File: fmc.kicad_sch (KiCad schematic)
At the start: 2 parts, among them P1 ASP-134604-01, P2 ASP-134604-01

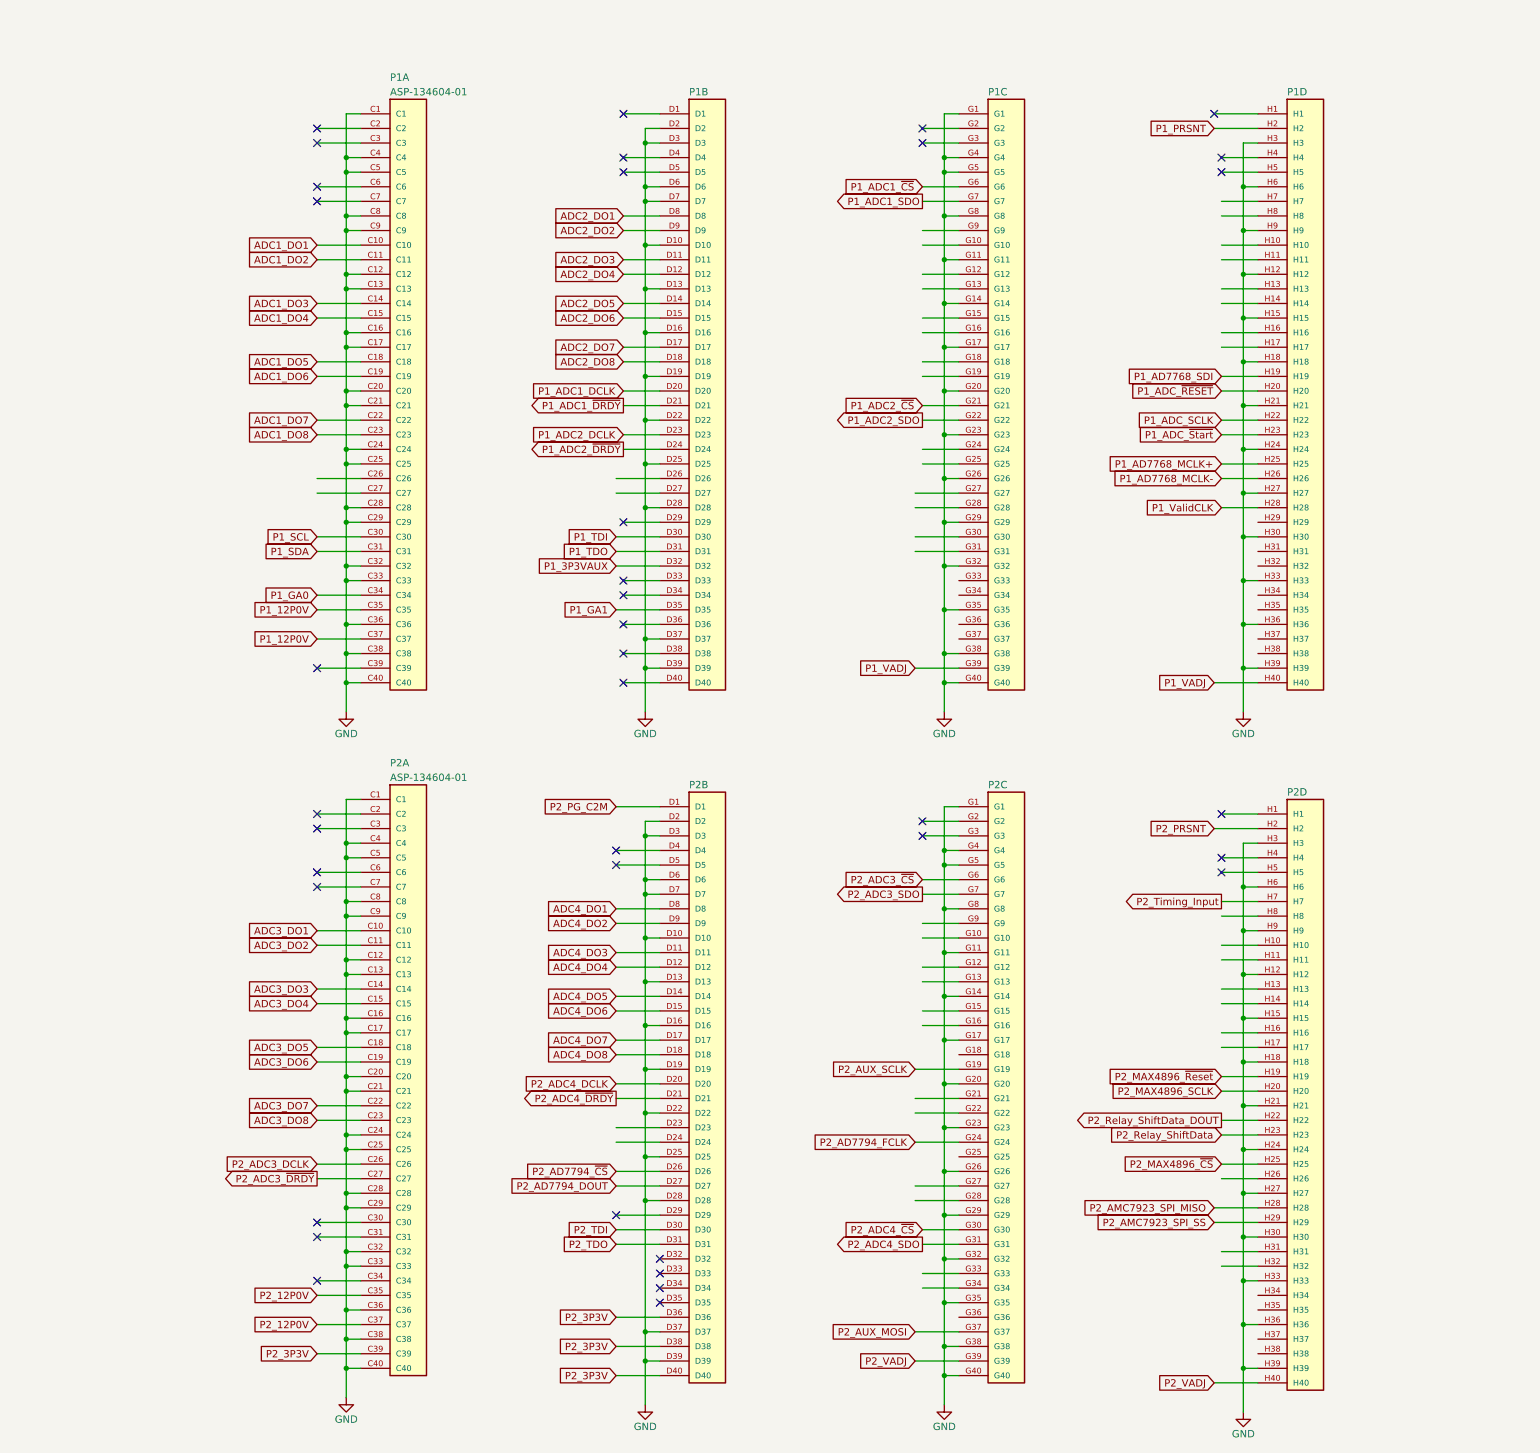
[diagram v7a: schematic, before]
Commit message: Schematic Updates
Updated:
-Fixed AMC7823 labels
-Added present detect signals on FMC
-Added ferrite beads in Power Section and AFE
-Added 0R in power section
-Revised EEPROM connections
-Changed +5V SMPS part to one with an integrated inductor
-Added more detail on FMC connector
-Added file showing SMPS calculations
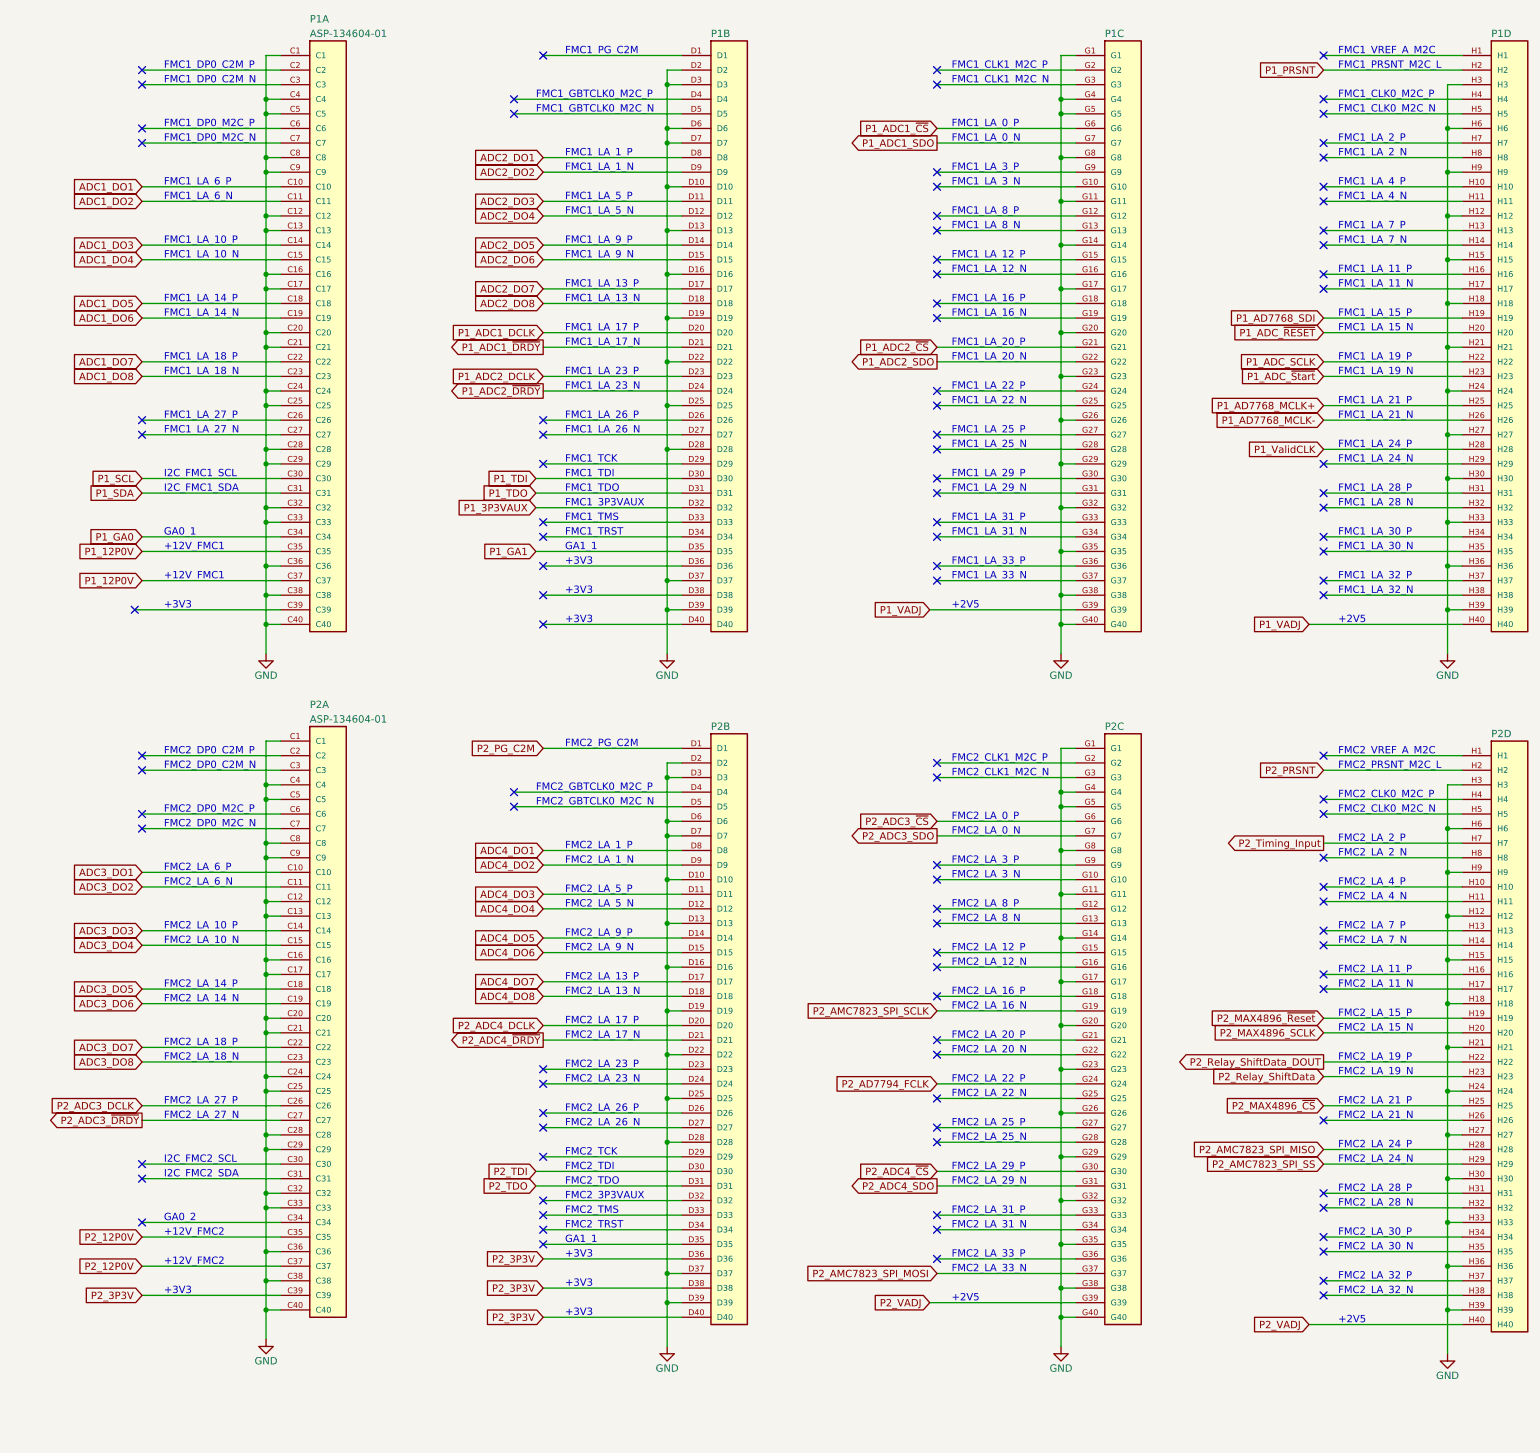
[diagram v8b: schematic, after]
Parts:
- P1, P2: MPN (none) -> ASP-134604-01
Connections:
- net P2_AD7794_DOUT: no longer names the net of P2.D27
- net P2_AD7794_~{CS}: no longer names the net of P2.D26
- net P2_AMC7923_SPI_MISO renamed P2_AMC7823_SPI_MISO
- net P2_AMC7923_SPI_SS renamed P2_AMC7823_SPI_SS
- net P2_AUX_MOSI renamed P2_AMC7823_SPI_MOSI
- net P2_AUX_SCLK renamed P2_AMC7823_SPI_SCLK
- no-connect marks 38 -> 108
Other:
- note added: "+12V_FMC1"
- note added: "+12V_FMC2"
- note added: "+2V5"
- note added: "+3V3"
- note added: "FMC1_3P3VAUX"
- note added: "FMC1_CLK0_M2C_N"
- note added: "FMC1_CLK0_M2C_P"
- note added: "FMC1_CLK1_M2C_N"
- note added: "FMC1_CLK1_M2C_P"
- note added: "FMC1_DP0_C2M_N"
- note added: "FMC1_DP0_C2M_P"
- note added: "FMC1_DP0_M2C_N"
- note added: "FMC1_DP0_M2C_P"
- note added: "FMC1_GBTCLK0_M2C_N"
- note added: "FMC1_GBTCLK0_M2C_P"
- note added: "FMC1_LA_0_N"
- note added: "FMC1_LA_0_P"
- note added: "FMC1_LA_10_N"
- note added: "FMC1_LA_10_P"
- note added: "FMC1_LA_11_N"
- note added: "FMC1_LA_11_P"
- note added: "FMC1_LA_12_N"
- note added: "FMC1_LA_12_P"
- note added: "FMC1_LA_13_N"
- note added: "FMC1_LA_13_P"
- note added: "FMC1_LA_14_N"
- note added: "FMC1_LA_14_P"
- note added: "FMC1_LA_15_N"
- note added: "FMC1_LA_15_P"
- note added: "FMC1_LA_16_N"
- note added: "FMC1_LA_16_P"
- note added: "FMC1_LA_17_N"
- note added: "FMC1_LA_17_P"
- note added: "FMC1_LA_18_N"
- note added: "FMC1_LA_18_P"
- note added: "FMC1_LA_19_N"
- note added: "FMC1_LA_19_P"
- note added: "FMC1_LA_1_N"
- note added: "FMC1_LA_1_P"
- note added: "FMC1_LA_20_N"
- note added: "FMC1_LA_20_P"
- note added: "FMC1_LA_21_N"
- note added: "FMC1_LA_21_P"
- note added: "FMC1_LA_22_N"
- note added: "FMC1_LA_22_P"
- note added: "FMC1_LA_23_N"
- note added: "FMC1_LA_23_P"
- note added: "FMC1_LA_24_N"
- note added: "FMC1_LA_24_P"
- note added: "FMC1_LA_25_N"
- note added: "FMC1_LA_25_P"
- note added: "FMC1_LA_26_N"
- note added: "FMC1_LA_26_P"
- note added: "FMC1_LA_27_N"
- note added: "FMC1_LA_27_P"
- note added: "FMC1_LA_28_N"
- note added: "FMC1_LA_28_P"
- note added: "FMC1_LA_29_N"
- note added: "FMC1_LA_29_P"
- note added: "FMC1_LA_2_N"
- note added: "FMC1_LA_2_P"
- note added: "FMC1_LA_30_N"
- note added: "FMC1_LA_30_P"
- note added: "FMC1_LA_31_N"
- note added: "FMC1_LA_31_P"
- note added: "FMC1_LA_32_N"
- note added: "FMC1_LA_32_P"
- note added: "FMC1_LA_33_N"
- note added: "FMC1_LA_33_P"
- note added: "FMC1_LA_3_N"
- note added: "FMC1_LA_3_P"
- note added: "FMC1_LA_4_N"
- note added: "FMC1_LA_4_P"
- note added: "FMC1_LA_5_N"
- note added: "FMC1_LA_5_P"
- note added: "FMC1_LA_6_N"
- note added: "FMC1_LA_6_P"
- note added: "FMC1_LA_7_N"
- note added: "FMC1_LA_7_P"
- note added: "FMC1_LA_8_N"
- note added: "FMC1_LA_8_P"
- note added: "FMC1_LA_9_N"
- note added: "FMC1_LA_9_P"
- note added: "FMC1_PG_C2M"
- note added: "FMC1_PRSNT_M2C_L"
- note added: "FMC1_TCK"
- note added: "FMC1_TDI"
- note added: "FMC1_TDO"
- note added: "FMC1_TMS"
- note added: "FMC1_TRST"
- note added: "FMC1_VREF_A_M2C"
- note added: "FMC2_3P3VAUX"
- note added: "FMC2_CLK0_M2C_N"
- note added: "FMC2_CLK0_M2C_P"
- note added: "FMC2_CLK1_M2C_N"
- note added: "FMC2_CLK1_M2C_P"
- note added: "FMC2_DP0_C2M_N"
- note added: "FMC2_DP0_C2M_P"
- note added: "FMC2_DP0_M2C_N"
- note added: "FMC2_DP0_M2C_P"
- note added: "FMC2_GBTCLK0_M2C_N"
- note added: "FMC2_GBTCLK0_M2C_P"
- note added: "FMC2_LA_0_N"
- note added: "FMC2_LA_0_P"
- note added: "FMC2_LA_10_N"
- note added: "FMC2_LA_10_P"
- note added: "FMC2_LA_11_N"
- note added: "FMC2_LA_11_P"
- note added: "FMC2_LA_12_N"
- note added: "FMC2_LA_12_P"
- note added: "FMC2_LA_13_N"
- note added: "FMC2_LA_13_P"
- note added: "FMC2_LA_14_N"
- note added: "FMC2_LA_14_P"
- note added: "FMC2_LA_15_N"
- note added: "FMC2_LA_15_P"
- note added: "FMC2_LA_16_N"
- note added: "FMC2_LA_16_P"
- note added: "FMC2_LA_17_N"
- note added: "FMC2_LA_17_P"
- note added: "FMC2_LA_18_N"
- note added: "FMC2_LA_18_P"
- note added: "FMC2_LA_19_N"
- note added: "FMC2_LA_19_P"
- note added: "FMC2_LA_1_N"
- note added: "FMC2_LA_1_P"
- note added: "FMC2_LA_20_N"
- note added: "FMC2_LA_20_P"
- note added: "FMC2_LA_21_N"
- note added: "FMC2_LA_21_P"
- note added: "FMC2_LA_22_N"
- note added: "FMC2_LA_22_P"
- note added: "FMC2_LA_23_N"
- note added: "FMC2_LA_23_P"
- note added: "FMC2_LA_24_N"
- note added: "FMC2_LA_24_P"
- note added: "FMC2_LA_25_N"
- note added: "FMC2_LA_25_P"
- note added: "FMC2_LA_26_N"
- note added: "FMC2_LA_26_P"
- note added: "FMC2_LA_27_N"
- note added: "FMC2_LA_27_P"
- note added: "FMC2_LA_28_N"
- note added: "FMC2_LA_28_P"
- note added: "FMC2_LA_29_N"
- note added: "FMC2_LA_29_P"
- note added: "FMC2_LA_2_N"
- note added: "FMC2_LA_2_P"
- note added: "FMC2_LA_30_N"
- note added: "FMC2_LA_30_P"
- note added: "FMC2_LA_31_N"
- note added: "FMC2_LA_31_P"
- note added: "FMC2_LA_32_N"
- note added: "FMC2_LA_32_P"
- note added: "FMC2_LA_33_N"
- note added: "FMC2_LA_33_P"
- note added: "FMC2_LA_3_N"
- note added: "FMC2_LA_3_P"
- note added: "FMC2_LA_4_N"
- note added: "FMC2_LA_4_P"
- note added: "FMC2_LA_5_N"
- note added: "FMC2_LA_5_P"
- note added: "FMC2_LA_6_N"
- note added: "FMC2_LA_6_P"
- note added: "FMC2_LA_7_N"
- note added: "FMC2_LA_7_P"
- note added: "FMC2_LA_8_N"
- note added: "FMC2_LA_8_P"
- note added: "FMC2_LA_9_N"
- note added: "FMC2_LA_9_P"
- note added: "FMC2_PG_C2M"
- note added: "FMC2_PRSNT_M2C_L"
- note added: "FMC2_TCK"
- note added: "FMC2_TDI"
- note added: "FMC2_TDO"
- note added: "FMC2_TMS"
- note added: "FMC2_TRST"
- note added: "FMC2_VREF_A_M2C"
- note added: "GA0_1"
- note added: "GA0_2"
- note added: "GA1_1"
- note added: "I2C_FMC1_SCL"
- note added: "I2C_FMC1_SDA"
- note added: "I2C_FMC2_SCL"
- note added: "I2C_FMC2_SDA"
- moved on the sheet: P1A, P1B, P1C, P1D, P2A, P2B, P2C, P2D
